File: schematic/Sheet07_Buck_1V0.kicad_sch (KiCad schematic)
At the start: 14 parts, among them U5 TPS7H5001-SP

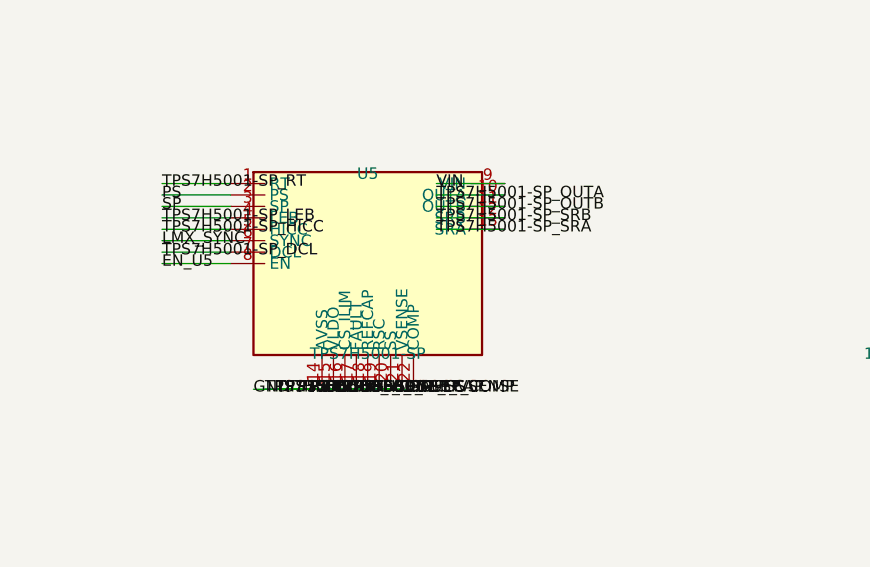
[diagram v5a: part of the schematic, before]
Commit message: fix: replace wire stubs with labels-only to prevent power net shorts
Labels placed directly at pin endpoints eliminate wire overlap that
caused BGA power pins (VA11, VA19, VD11, AGND, DGND) to merge into
a single net. Verified via netlist: GND=52, +1V0_ANA=12, +1V9_ANA=12,
+1V1_DIG=10 nodes (all correct per datasheet pin mapping).
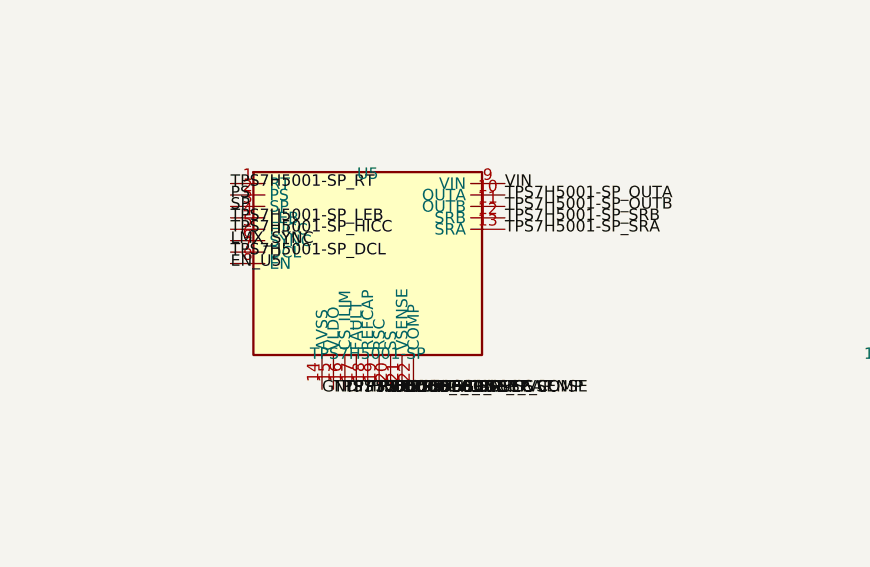
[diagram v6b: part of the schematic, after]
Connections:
- net GND: no longer U5.15 (VLDO), U5.16 (CS_ILIM), U5.17 (FAULT), U5.18 (REFCAP), U5.19 (RSC), U5.20 (SS), U5.21 (VSENSE), U5.22 (COMP)
- new net RSC: U5.19 (RSC)
- new net TPS7H5001-SP_COMP: U5.22 (COMP)
- new net TPS7H5001-SP_CS: U5.16 (CS_ILIM)
- new net TPS7H5001-SP_FAULT: U5.17 (FAULT)
- new net TPS7H5001-SP_REFCAP: U5.18 (REFCAP)
- new net TPS7H5001-SP_SS: U5.20 (SS)
- new net TPS7H5001-SP_VLDO: U5.15 (VLDO)
- new net TPS7H5001-SP_VSENSE: U5.21 (VSENSE)
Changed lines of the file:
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@@
     (pin "2")
   )
-  (wire (pts (xy 184.7600 91.1100) (xy 177.1400 91.1100)) (stroke (width 0) (type default)))
-  (label "TPS7H5001-SP_RT" (at 177.1400 91.1100 0) (effects (font (size 1.27 1.27))))
-  (wire (pts (xy 184.7600 92.3800) (xy 177.1400 92.3800)) (stroke (width 0) (type default)))
-  (label "PS" (at 177.1400 92.3800 0) (effects (font (size 1.27 1.27))))
-  (wire (pts (xy 184.7600 93.6500) (xy 177.1400 93.6500)) (stroke (width 0) (type default)))
-  (label "SP" (at 177.1400 93.6500 0) (effects (font (size 1.27 1.27))))
-  (wire (pts (xy 184.7600 94.9200) (xy 177.1400 94.9200)) (stroke (width 0) (type default)))
-  (label "TPS7H5001-SP_LEB" (at 177.1400 94.9200 0) (effects (font (size 1.27 1.27))))
-  (wire (pts (xy 184.7600 96.1900) (xy 177.1400 96.1900)) (stroke (width 0) (type default)))
-  (label "TPS7H5001-SP_HICC" (at 177.1400 96.1900 0) (effects (font (size 1.27 1.27))))
-  (wire (pts (xy 184.7600 97.4600) (xy 177.1400 97.4600)) (stroke (width 0) (type default)))
-  (label "LMX_SYNC" (at 177.1400 97.4600 0) (effects (font (size 1.27 1.27))))
-  (wire (pts (xy 184.7600 98.7300) (xy 177.1400 98.7300)) (stroke (width 0) (type default)))
-  (label "TPS7H5001-SP_DCL" (at 177.1400 98.7300 0) (effects (font (size 1.27 1.27))))
-  (wire (pts (xy 184.7600 100.0000) (xy 177.1400 100.0000)) (stroke (width 0) (type default)))
-  (label "EN_U5" (at 177.1400 100.0000 0) (effects (font (size 1.27 1.27))))
-  (wire (pts (xy 215.2400 91.1100) (xy 207.6200 91.1100)) (stroke (width 0) (type default)))
-  (label "VIN" (at 207.6200 91.1100 0) (effects (font (size 1.27 1.27))))
-  (wire (pts (xy 215.2400 92.3800) (xy 207.6200 92.3800)) (stroke (width 0) (type default)))
-  (label "TPS7H5001-SP_OUTA" (at 207.6200 92.3800 0) (effects (font (size 1.27 1.27))))
-  (wire (pts (xy 215.2400 93.6500) (xy 207.6200 93.6500)) (stroke (width 0) (type default)))
-  (label "TPS7H5001-SP_OUTB" (at 207.6200 93.6500 0) (effects (font (size 1.27 1.27))))
-  (wire (pts (xy 215.2400 94.9200) (xy 207.6200 94.9200)) (stroke (width 0) (type default)))
-  (label "TPS7H5001-SP_SRB" (at 207.6200 94.9200 0) (effects (font (size 1.27 1.27))))
-  (wire (pts (xy 215.2400 96.1900) (xy 207.6200 96.1900)) (stroke (width 0) (type default)))
-  (label "TPS7H5001-SP_SRA" (at 207.6200 96.1900 0) (effects (font (size 1.27 1.27))))
-  (wire (pts (xy 194.9200 113.9700) (xy 187.3000 113.9700)) (stroke (width 0) (type default)))
-  (label "GND" (at 187.3000 113.9700 0) (effects (font (size 1.27 1.27))))
-  (wire (pts (xy 196.1900 113.9700) (xy 188.5700 113.9700)) (stroke (width 0) (type default)))
-  (label "TPS7H5001-SP_VLDO" (at 188.5700 113.9700 0) (effects (font (size 1.27 1.27))))
-  (wire (pts (xy 197.4600 113.9700) (xy 189.8400 113.9700)) (stroke (width 0) (type default)))
-  (label "TPS7H5001-SP_CS" (at 189.8400 113.9700 0) (effects (font (size 1.27 1.27))))
-  (wire (pts (xy 198.7300 113.9700) (xy 191.1100 113.9700)) (stroke (width 0) (type default)))
-  (label "TPS7H5001-SP_FAULT" (at 191.1100 113.9700 0) (effects (font (size 1.27 1.27))))
-  (wire (pts (xy 200.0000 113.9700) (xy 192.3800 113.9700)) (stroke (width 0) (type default)))
-  (label "TPS7H5001-SP_REFCAP" (at 192.3800 113.9700 0) (effects (font (size 1.27 1.27))))
-  (wire (pts (xy 201.2700 113.9700) (xy 193.6500 113.9700)) (stroke (width 0) (type default)))
-  (label "RSC" (at 193.6500 113.9700 0) (effects (font (size 1.27 1.27))))
-  (wire (pts (xy 202.5400 113.9700) (xy 194.9200 113.9700)) (stroke (width 0) (type default)))
-  (label "TPS7H5001-SP_SS" (at 194.9200 113.9700 0) (effects (font (size 1.27 1.27))))
-  (wire (pts (xy 203.8100 113.9700) (xy 196.1900 113.9700)) (stroke (width 0) (type default)))
-  (label "TPS7H5001-SP_VSENSE" (at 196.1900 113.9700 0) (effects (font (size 1.27 1.27))))
-  (wire (pts (xy 205.0800 113.9700) (xy 197.4600 113.9700)) (stroke (width 0) (type default)))
-  (label "TPS7H5001-SP_COMP" (at 197.4600 113.9700 0) (effects (font (size 1.27 1.27))))
+  (label "TPS7H5001-SP_RT" (at 184.7600 91.1100 0) (effects (font (size 1.27 1.27))))
+  (label "PS" (at 184.7600 92.3800 0) (effects (font (size 1.27 1.27))))
+  (label "SP" (at 184.7600 93.6500 0) (effects (font (size 1.27 1.27))))
+  (label "TPS7H5001-SP_LEB" (at 184.7600 94.9200 0) (effects (font (size 1.27 1.27))))
+  (label "TPS7H5001-SP_HICC" (at 184.7600 96.1900 0) (effects (font (size 1.27 1.27))))
+  (label "LMX_SYNC" (at 184.7600 97.4600 0) (effects (font (size 1.27 1.27))))
+  (label "TPS7H5001-SP_DCL" (at 184.7600 98.7300 0) (effects (font (size 1.27 1.27))))
+  (label "EN_U5" (at 184.7600 100.0000 0) (effects (font (size 1.27 1.27))))
+  (label "VIN" (at 215.2400 91.1100 0) (effects (font (size 1.27 1.27))))
+  (label "TPS7H5001-SP_OUTA" (at 215.2400 92.3800 0) (effects (font (size 1.27 1.27))))
+  (label "TPS7H5001-SP_OUTB" (at 215.2400 93.6500 0) (effects (font (size 1.27 1.27))))
+  (label "TPS7H5001-SP_SRB" (at 215.2400 94.9200 0) (effects (font (size 1.27 1.27))))
+  (label "TPS7H5001-SP_SRA" (at 215.2400 96.1900 0) (effects (font (size 1.27 1.27))))
+  (label "GND" (at 194.9200 113.9700 0) (effects (font (size 1.27 1.27))))
+  (label "TPS7H5001-SP_VLDO" (at 196.1900 113.9700 0) (effects (font (size 1.27 1.27))))
+  (label "TPS7H5001-SP_CS" (at 197.4600 113.9700 0) (effects (font (size 1.27 1.27))))
+  (label "TPS7H5001-SP_FAULT" (at 198.7300 113.9700 0) (effects (font (size 1.27 1.27))))
+  (label "TPS7H5001-SP_REFCAP" (at 200.0000 113.9700 0) (effects (font (size 1.27 1.27))))
+  (label "RSC" (at 201.2700 113.9700 0) (effects (font (size 1.27 1.27))))
+  (label "TPS7H5001-SP_SS" (at 202.5400 113.9700 0) (effects (font (size 1.27 1.27))))
+  (label "TPS7H5001-SP_VSENSE" (at 203.8100 113.9700 0) (effects (font (size 1.27 1.27))))
+  (label "TPS7H5001-SP_COMP" (at 205.0800 113.9700 0) (effects (font (size 1.27 1.27))))
   (sheet_instances (path "/" (page "1")))
 )

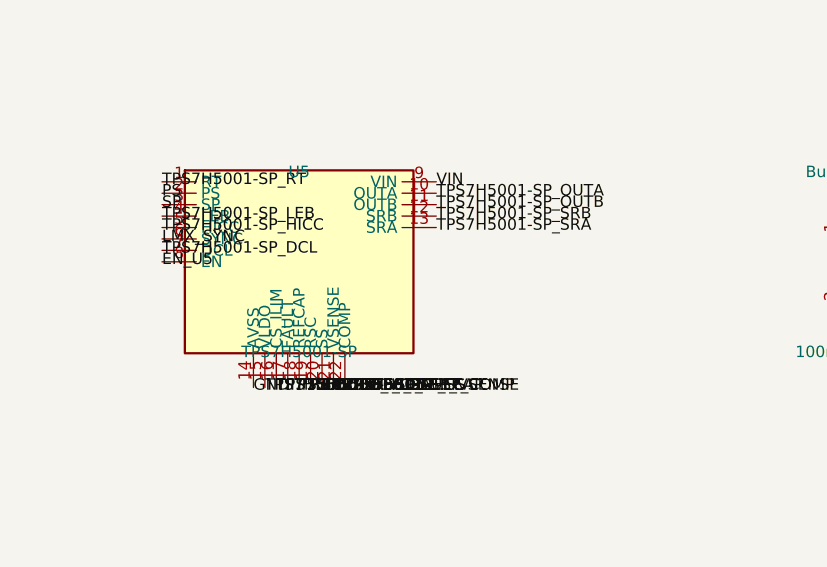
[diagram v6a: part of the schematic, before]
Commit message: fix: isolate ISL70003ASEH buck pins, fix LMX_SYNC collision, NC pins, connector pin names
- ISL70003ASEH pins now use ref prefix (U6_LX1 vs U7_LX1) to prevent shorts
- Buck SYNC pins separated from LMX_SYNC (power sync ≠ PLL sync)
- NC pins properly skipped (unconnected)
- Connector PIN_1..PIN_6 use ref prefix (J1_PIN_1 vs J2_PIN_1)
- Fixed annotation warnings in Sheet13 (C_dev→C125, R_dev→R74, U_TPS7H→U14)
- Regenerated all PDFs and SVGs
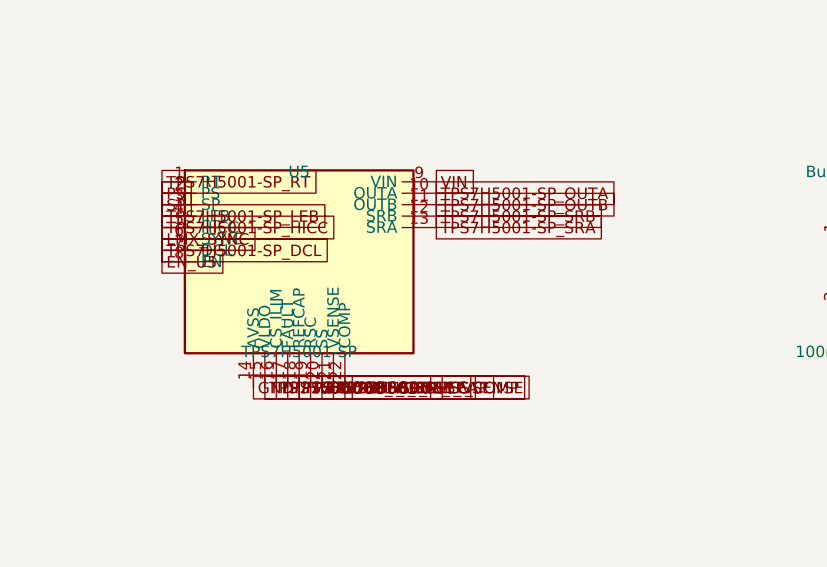
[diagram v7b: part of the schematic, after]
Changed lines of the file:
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@@
     (pin "2")
   )
-  (label "TPS7H5001-SP_RT" (at 184.7600 91.1100 0) (effects (font (size 1.27 1.27))))
-  (label "PS" (at 184.7600 92.3800 0) (effects (font (size 1.27 1.27))))
-  (label "SP" (at 184.7600 93.6500 0) (effects (font (size 1.27 1.27))))
-  (label "TPS7H5001-SP_LEB" (at 184.7600 94.9200 0) (effects (font (size 1.27 1.27))))
-  (label "TPS7H5001-SP_HICC" (at 184.7600 96.1900 0) (effects (font (size 1.27 1.27))))
-  (label "LMX_SYNC" (at 184.7600 97.4600 0) (effects (font (size 1.27 1.27))))
-  (label "TPS7H5001-SP_DCL" (at 184.7600 98.7300 0) (effects (font (size 1.27 1.27))))
-  (label "EN_U5" (at 184.7600 100.0000 0) (effects (font (size 1.27 1.27))))
-  (label "VIN" (at 215.2400 91.1100 0) (effects (font (size 1.27 1.27))))
-  (label "TPS7H5001-SP_OUTA" (at 215.2400 92.3800 0) (effects (font (size 1.27 1.27))))
-  (label "TPS7H5001-SP_OUTB" (at 215.2400 93.6500 0) (effects (font (size 1.27 1.27))))
-  (label "TPS7H5001-SP_SRB" (at 215.2400 94.9200 0) (effects (font (size 1.27 1.27))))
-  (label "TPS7H5001-SP_SRA" (at 215.2400 96.1900 0) (effects (font (size 1.27 1.27))))
-  (label "GND" (at 194.9200 113.9700 0) (effects (font (size 1.27 1.27))))
-  (label "TPS7H5001-SP_VLDO" (at 196.1900 113.9700 0) (effects (font (size 1.27 1.27))))
-  (label "TPS7H5001-SP_CS" (at 197.4600 113.9700 0) (effects (font (size 1.27 1.27))))
-  (label "TPS7H5001-SP_FAULT" (at 198.7300 113.9700 0) (effects (font (size 1.27 1.27))))
-  (label "TPS7H5001-SP_REFCAP" (at 200.0000 113.9700 0) (effects (font (size 1.27 1.27))))
-  (label "RSC" (at 201.2700 113.9700 0) (effects (font (size 1.27 1.27))))
-  (label "TPS7H5001-SP_SS" (at 202.5400 113.9700 0) (effects (font (size 1.27 1.27))))
-  (label "TPS7H5001-SP_VSENSE" (at 203.8100 113.9700 0) (effects (font (size 1.27 1.27))))
-  (label "TPS7H5001-SP_COMP" (at 205.0800 113.9700 0) (effects (font (size 1.27 1.27))))
+  (global_label "TPS7H5001-SP_RT" (at 184.7600 91.1100 0) (effects (font (size 1.27 1.27))))
+  (global_label "PS" (at 184.7600 92.3800 0) (effects (font (size 1.27 1.27))))
+  (global_label "SP" (at 184.7600 93.6500 0) (effects (font (size 1.27 1.27))))
+  (global_label "TPS7H5001-SP_LEB" (at 184.7600 94.9200 0) (effects (font (size 1.27 1.27))))
+  (global_label "TPS7H5001-SP_HICC" (at 184.7600 96.1900 0) (effects (font (size 1.27 1.27))))
+  (global_label "LMX_SYNC" (at 184.7600 97.4600 0) (effects (font (size 1.27 1.27))))
+  (global_label "TPS7H5001-SP_DCL" (at 184.7600 98.7300 0) (effects (font (size 1.27 1.27))))
+  (global_label "EN_U5" (at 184.7600 100.0000 0) (effects (font (size 1.27 1.27))))
+  (global_label "VIN" (at 215.2400 91.1100 0) (effects (font (size 1.27 1.27))))
+  (global_label "TPS7H5001-SP_OUTA" (at 215.2400 92.3800 0) (effects (font (size 1.27 1.27))))
+  (global_label "TPS7H5001-SP_OUTB" (at 215.2400 93.6500 0) (effects (font (size 1.27 1.27))))
+  (global_label "TPS7H5001-SP_SRB" (at 215.2400 94.9200 0) (effects (font (size 1.27 1.27))))
+  (global_label "TPS7H5001-SP_SRA" (at 215.2400 96.1900 0) (effects (font (size 1.27 1.27))))
+  (global_label "GND" (at 194.9200 113.9700 0) (effects (font (size 1.27 1.27))))
+  (global_label "TPS7H5001-SP_VLDO" (at 196.1900 113.9700 0) (effects (font (size 1.27 1.27))))
+  (global_label "TPS7H5001-SP_CS" (at 197.4600 113.9700 0) (effects (font (size 1.27 1.27))))
+  (global_label "TPS7H5001-SP_FAULT" (at 198.7300 113.9700 0) (effects (font (size 1.27 1.27))))
+  (global_label "TPS7H5001-SP_REFCAP" (at 200.0000 113.9700 0) (effects (font (size 1.27 1.27))))
+  (global_label "RSC" (at 201.2700 113.9700 0) (effects (font (size 1.27 1.27))))
+  (global_label "TPS7H5001-SP_SS" (at 202.5400 113.9700 0) (effects (font (size 1.27 1.27))))
+  (global_label "TPS7H5001-SP_VSENSE" (at 203.8100 113.9700 0) (effects (font (size 1.27 1.27))))
+  (global_label "TPS7H5001-SP_COMP" (at 205.0800 113.9700 0) (effects (font (size 1.27 1.27))))
   (sheet_instances (path "/" (page "1")))
 )
